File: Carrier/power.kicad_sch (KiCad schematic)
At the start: 49 parts, among them J8 USB_C_Receptacle_USB2.0_16P, Q1 AO3400A, Q3 AO3400A, U10 EL817S1C, U12 USBLC6-2SC6, U2 IP5306, U9 EL817S1C

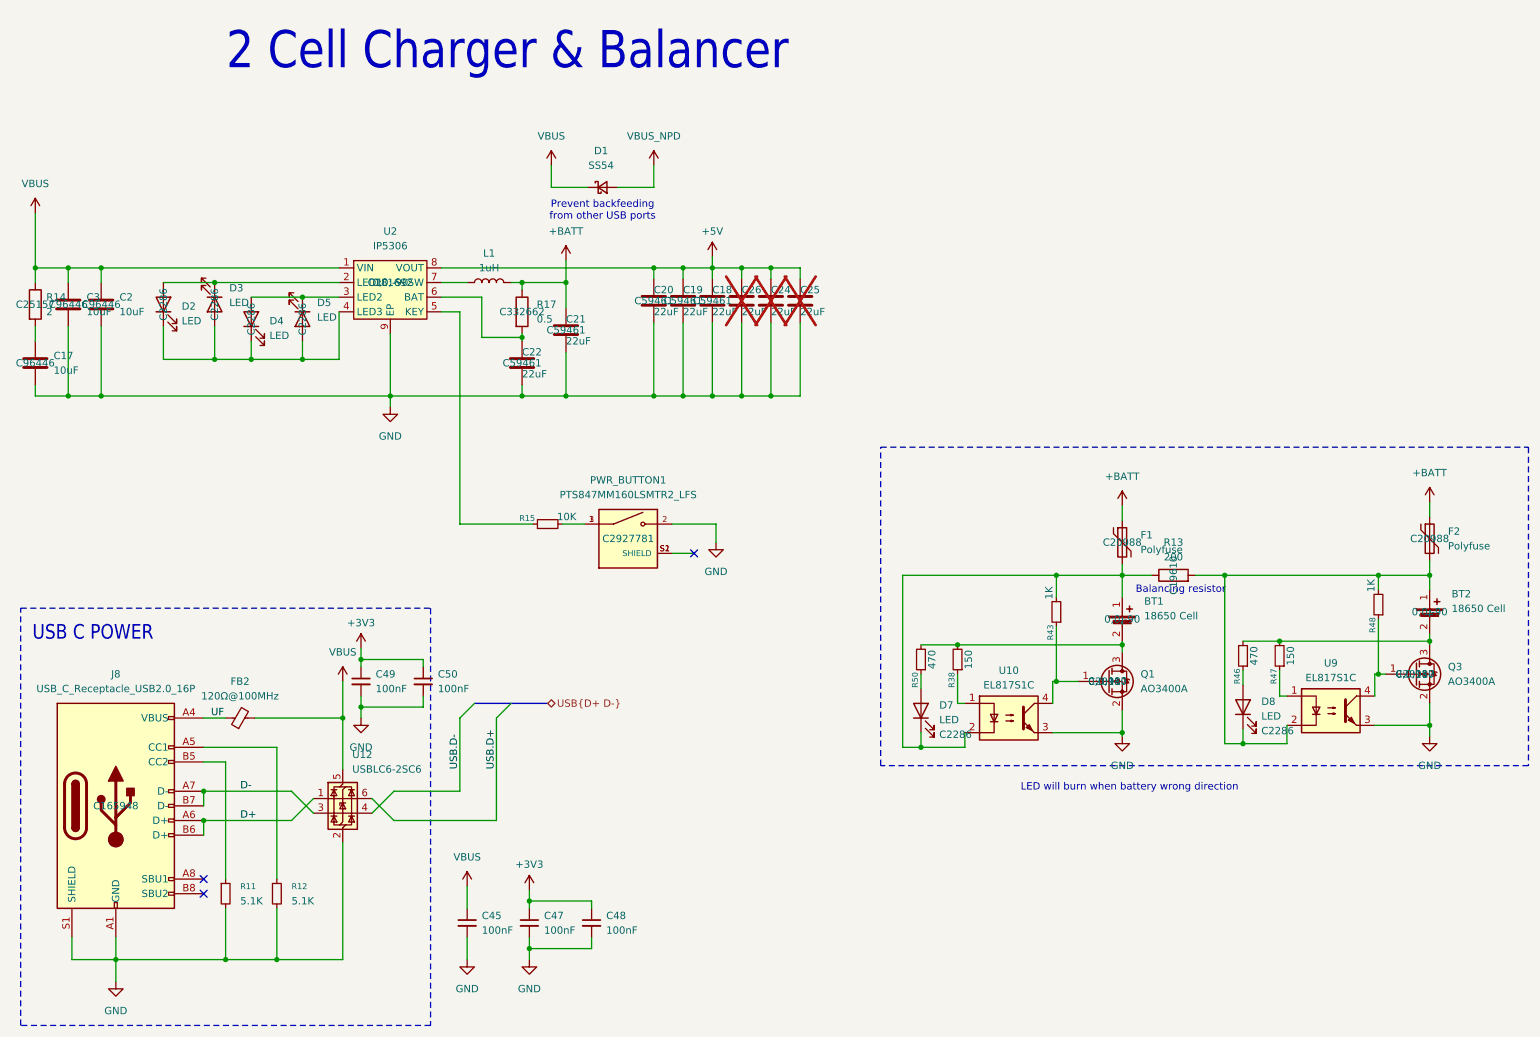
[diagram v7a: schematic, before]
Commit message: Rotated the 18650 cell / Wired it in. Wired out circuitry, placed flipper zero headers down.
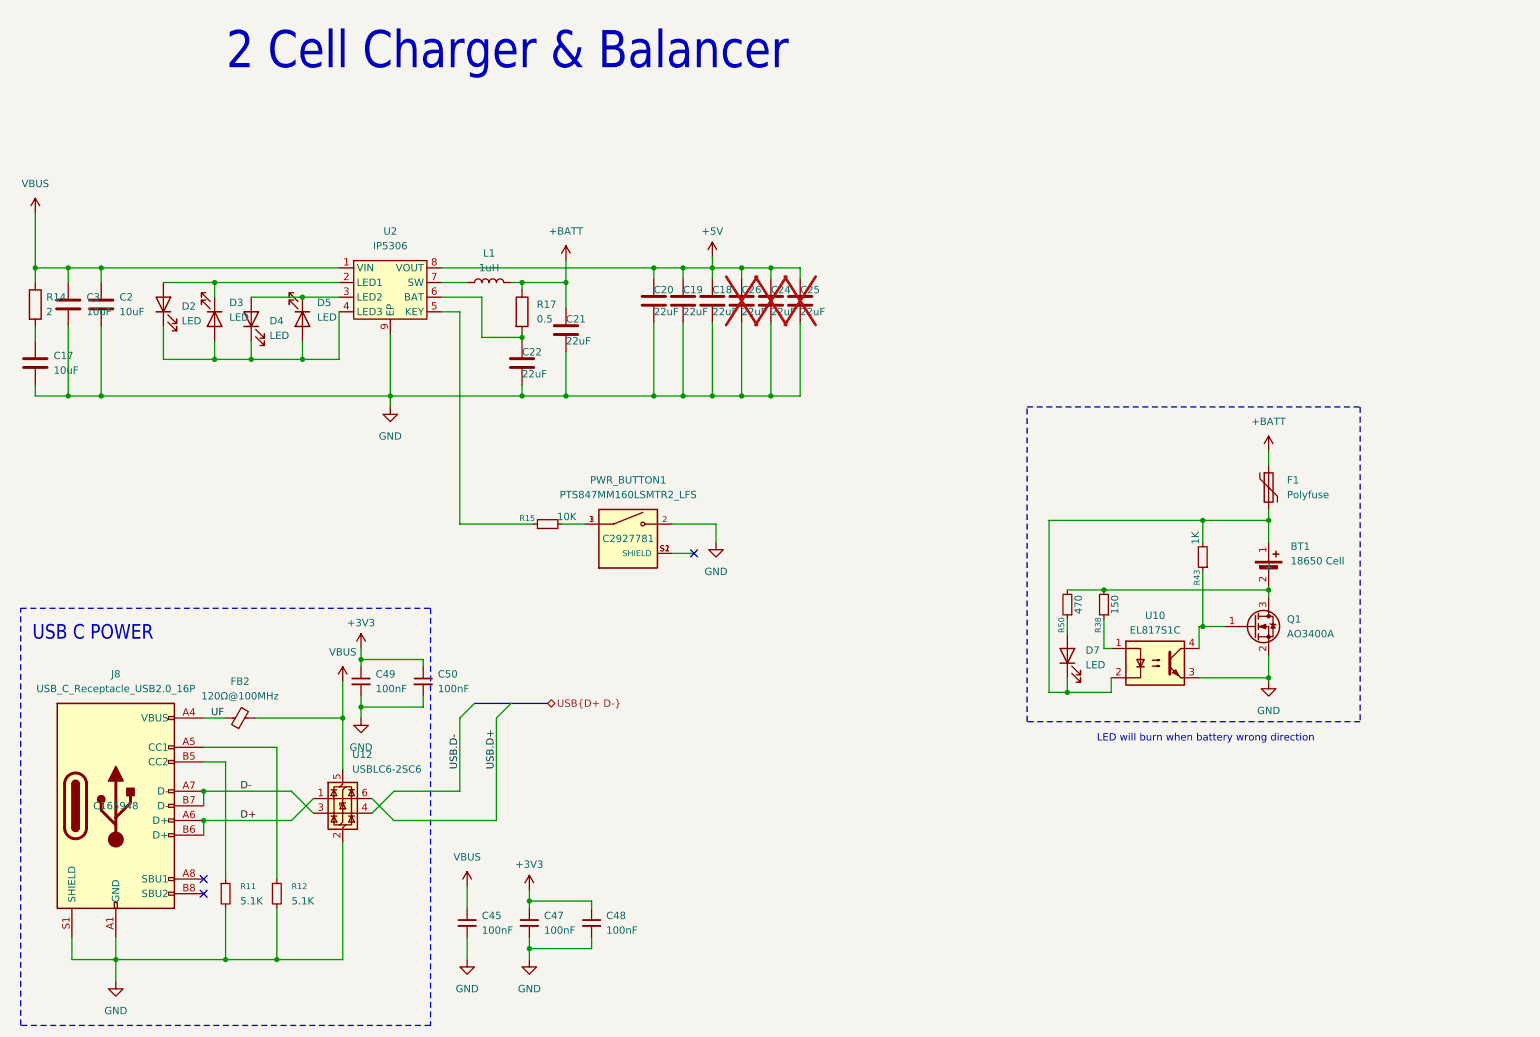
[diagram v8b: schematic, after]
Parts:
- removed BT2: 18650 Cell, BH-18650-B1BA002:BH-18650-B1BA002, symbol BH-18650-B1BA002:BH-18650-B1BA002
- removed D1: SS54, Diode_SMD:D_SMA, symbol Device:D_Schottky_Small
- removed D8: LED, LED_SMD:LED_0603_1608Metric, symbol Device:LED
- removed F2: Polyfuse, Fuse:Fuse_1206_3216Metric, symbol Device:Polyfuse
- removed Q3: AO3400A, Package_TO_SOT_SMD:SOT-23, symbol Transistor_FET:AO3400A
- removed R13: 200, Resistor_SMD:R_2010_5025Metric, symbol Device:R
- removed R46: 470, Resistor_SMD:R_0402_1005Metric, symbol Device:R_Small
- removed R47: 150, Resistor_SMD:R_0402_1005Metric, symbol Device:R_Small
- removed R48: 1K, Resistor_SMD:R_0402_1005Metric, symbol Device:R_Small
- removed U9: EL817S1C, EL817:SOIC254P1030X390-4N, symbol Isolator:EL817
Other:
- note removed: "Balancing resistor"
- note removed: "Prevent backfeeding from other USB ports"
- moved on the sheet: BT1, D3, D7, F1, Q1, R38, R43, R50, U10
